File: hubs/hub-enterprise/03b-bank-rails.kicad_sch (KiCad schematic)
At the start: 0 parts

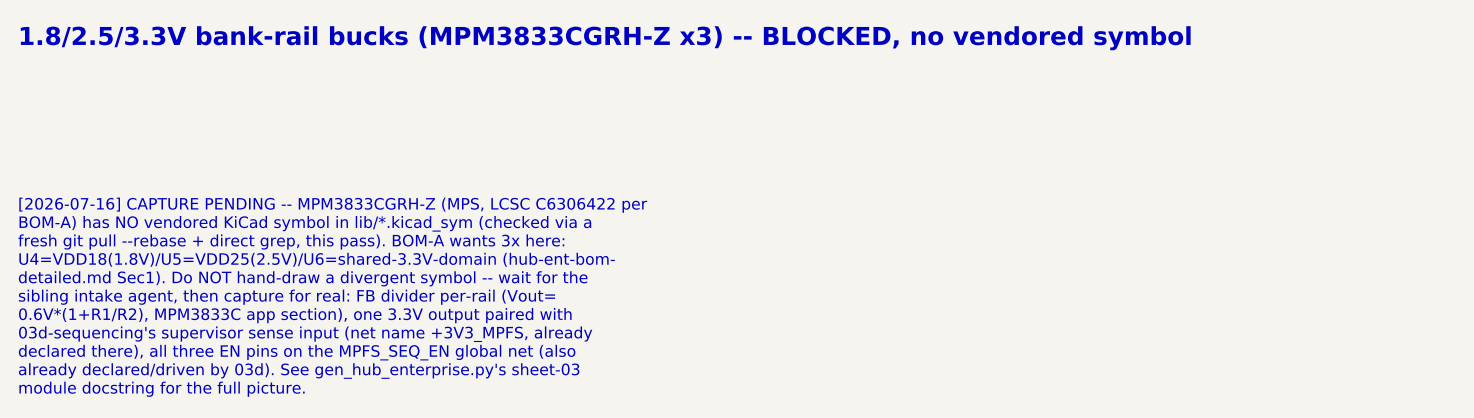
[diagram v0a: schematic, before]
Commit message: ENT hub: verify + finalize sheet 03 (compute-rails), extend MCP wishlist
Supersedes the automated WIP checkpoint d436d03c (taken mid-2026-07-16
platform outage to preserve in-flight work) with the actual verified
state. gen_hub_enterprise.py, scripts/check_hub_ent_sch.py, and the
shared-engine fixes in scripts/cec_sch_compose.py/cec_sch_layout.py
were already durable via that checkpoint; this commit lands the final
regenerated leaf content plus documentation, after a full post-outage
re-verification pass.

Sheet 03 (03-compute-rails): 03a-core-buck and 03d-sequencing are real
captures (MIC22705YML-TR core buck + TPS3839K33 sequencing supervisor,
cross-tied via the MPFS_SEQ_EN global net and the +3V3_MPFS forward-
declared root export); 03b-bank-rails and 03c-vdda-ldo remain honest
CAPTURE PENDING stubs (MPM3833CGRH-Z and the correct-voltage TPS7A20
variants are not yet vendored — see FOLLOWUPS.md).

Content change this commit: converted every multi-line schematic note
in the four sheet-03 leaves from a single embedded-newline string to
one `c.note()` call per line (new `multiline_note()` helper in
gen_hub_enterprise.py), sidestepping a real bug found this session in
the shared T1 engine: cec_sch_layout.py's `_unescape()` only ever
reversed `\"` and `\\`, never the literal `\n` cec_sch_compose.py's
emit_caption uses to store multi-line text — so every multi-line
note's width was measured as one giant line, silently inflating
`check_overlaps`/`check_sheet_bounds`. The proper engine-level fix for
`_unescape()` (and a companion `content_bbox` empty-leaf-crash fix)
were made this session too, but both are shared files outside this
agent's authorized staging scope; they reached history only via the
outage checkpoint, not this commit, and are not re-touched here.

Six-gate verification (this commit's final state):
1. ERC: 282 violations, all six classes (lib_symbol_mismatch 118,
   pin_not_connected 65, pin_to_pin 24, isolated_pin_label 71,
   pin_not_driven 3, power_pin_n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
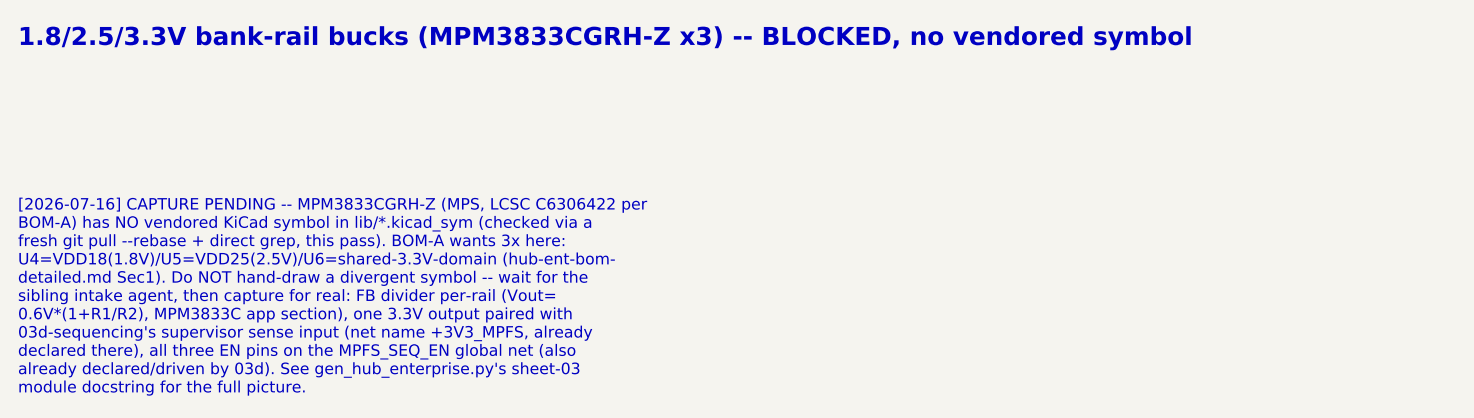
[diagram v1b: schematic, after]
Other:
- note added: "0.6V*(1+R1/R2), MPM3833C app section), one 3.3V output paired with"
- note added: "03d-sequencing's supervisor sense input (net name +3V3_MPFS, already"
- note added: "BOM-A) has NO vendored KiCad symbol in lib/*.kicad_sym (checked via a"
- note added: "U4=VDD18(1.8V)/U5=VDD25(2.5V)/U6=shared-3.3V-domain (hub-ent-bom-"
- note added: "[2026-07-16] CAPTURE PENDING -- MPM3833CGRH-Z (MPS, LCSC C6306422 per"
- note added: "already declared/driven by 03d). See gen_hub_enterprise.py's sheet-03"
- note added: "declared there), all three EN pins on the MPFS_SEQ_EN global net (also"
- note added: "detailed.md Sec1). Do NOT hand-draw a divergent symbol -- wait for the"
- note added: "fresh git pull --rebase + direct grep, this pass). BOM-A wants 3x here:"
- note added: "module docstring for the full picture."
- note added: "sibling intake agent, then capture for real: FB divider per-rail (Vout="
- note removed: "[2026-07-16] CAPTURE PENDING -- MPM3833CGRH-Z (MPS, LCSC C6306422 per BOM-A) has NO vendored KiCad symbol in lib/*.kicad_sym (checked via a fresh git pull --rebase + direct grep, this pass). BOM-A wants 3x here: U4=VDD18(1.8V)/U5=VDD25(2.5V)/U6=shared-3.3V-domain (hub-ent-bom- detailed.md Sec1). Do NOT hand-draw a divergent symbol -- wait for the sibling intake agent, then capture for real: FB di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"
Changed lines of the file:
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@@
 		(effects (font (size 2 2) (thickness 0.35) (bold yes) (color 26 95 180 1)) (justify left top))
 	)
-	(text "[2026-07-16] CAPTURE PENDING -- MPM3833CGRH-Z (MPS, LCSC C6306422 per\nBOM-A) has NO vendored KiCad symbol in lib/*.kicad_sym (checked via a\nfresh git pull --rebase + direct grep, this pass). BOM-A wants 3x here:\nU4=VDD18(1.8V)/U5=VDD25(2.5V)/U6=shared-3.3V-domain (hub-ent-bom-\ndetailed.md Sec1). Do NOT hand-draw a divergent symbol -- wait for the\nsibling intake agent, then capture for real: FB divider per-rail (Vout=\n0.6V*(1+R1/R2), MPM3833C app section), one 3.3V output paired with\n03d-sequencing's supervisor sense input (net name +3V3_MPFS, already\ndeclared there), all three EN pins on the MPFS_SEQ_EN global net (also\nalready declared/driven by 03d). See gen_hub_enterprise.py's sheet-03\nmodule docstring for the full picture."
+	(text "[2026-07-16] CAPTURE PENDING -- MPM3833CGRH-Z (MPS, LCSC C6306422 per"
 		(exclude_from_sim no)
 		(at 130.81 143.51 0)
 		(effects (font (size 1.27 1.27) (color 21 96 61 1)) (justify left top))
 	)
+	(text "BOM-A) has NO vendored KiCad symbol in lib/*.kicad_sym (checked via a"
+		(exclude_from_sim no)
+		(at 130.81 145.542 0)
+		(effects (font (size 1.27 1.27) (color 21 96 61 1)) (justify left top))
+	)
+	(text "fresh git pull --rebase + direct grep, this pass). BOM-A wants 3x here:"
+		(exclude_from_sim no)
+		(at 130.81 147.574 0)
+		(effects (font (size 1.27 1.27) (color 21 96 61 1)) (justify left top))
+	)
+	(text "U4=VDD18(1.8V)/U5=VDD25(2.5V)/U6=shared-3.3V-domain (hub-ent-bom-"
+		(exclude_from_sim no)
+		(at 130.81 149.606 0)
+		(effects (font (size 1.27 1.27) (color 21 96 61 1)) (justify left top))
+	)
+	(text "detailed.md Sec1). Do NOT hand-draw a divergent symbol -- wait for the"
+		(exclude_from_sim no)
+		(at 130.81 151.638 0)
+		(effects (font (size 1.27 1.27) (color 21 96 61 1)) (justify left top))
+	)
+	(text "sibling intake agent, then capture for real: FB divider per-rail (Vout="
+		(exclude_from_sim no)
+		(at 130.81 153.67 0)
+		(effects (font (size 1.27 1.27) (color 21 96 61 1)) (justify left top))
+	)
+	(text "0.6V*(1+R1/R2), MPM3833C app section), one 3.3V output paired with"
+		(exclude_from_sim no)
+		(at 130.81 155.702 0)
+		(effects (font (size 1.27 1.27) (color 21 96 61 1)) (justify left top))
+	)
+	(text "03d-sequencing's supervisor sense input (net name +3V3_MPFS, already"
+		(exclude_from_sim no)
+		(at 130.81 157.734 0)
+		(effects (font (size 1.27 1.27) (color 21 96 61 1)) (justify left top))
+	)
+	(text "declared there), all three EN pins on the MPFS_SEQ_EN global net (also"
+		(exclude_from_sim no)
+		(at 130.81 159.766 0)
+		(effects (font (size 1.27 1.27) (color 21 96 61 1)) (justify left top))
+	)
+	(text "already declared/driven by 03d). See gen_hub_enterprise.py's sheet-03"
+		(exclude_from_sim no)
+		(at 130.81 161.798 0)
+		(effects (font (size 1.27 1.27) (color 21 96 61 1)) (justify left top))
+	)
+	(text "module docstring for the full picture."
+		(exclude_from_sim no)
+		(at 130.81 163.83 0)
+		(effects (font (size 1.27 1.27) (color 21 96 61 1)) (justify left top))
+	)
